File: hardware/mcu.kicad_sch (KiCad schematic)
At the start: 27 parts, among them J6 Debug, SW1 BOOT, SW2 RESET, U3 STM32F405RGTx, Y1 8MHz

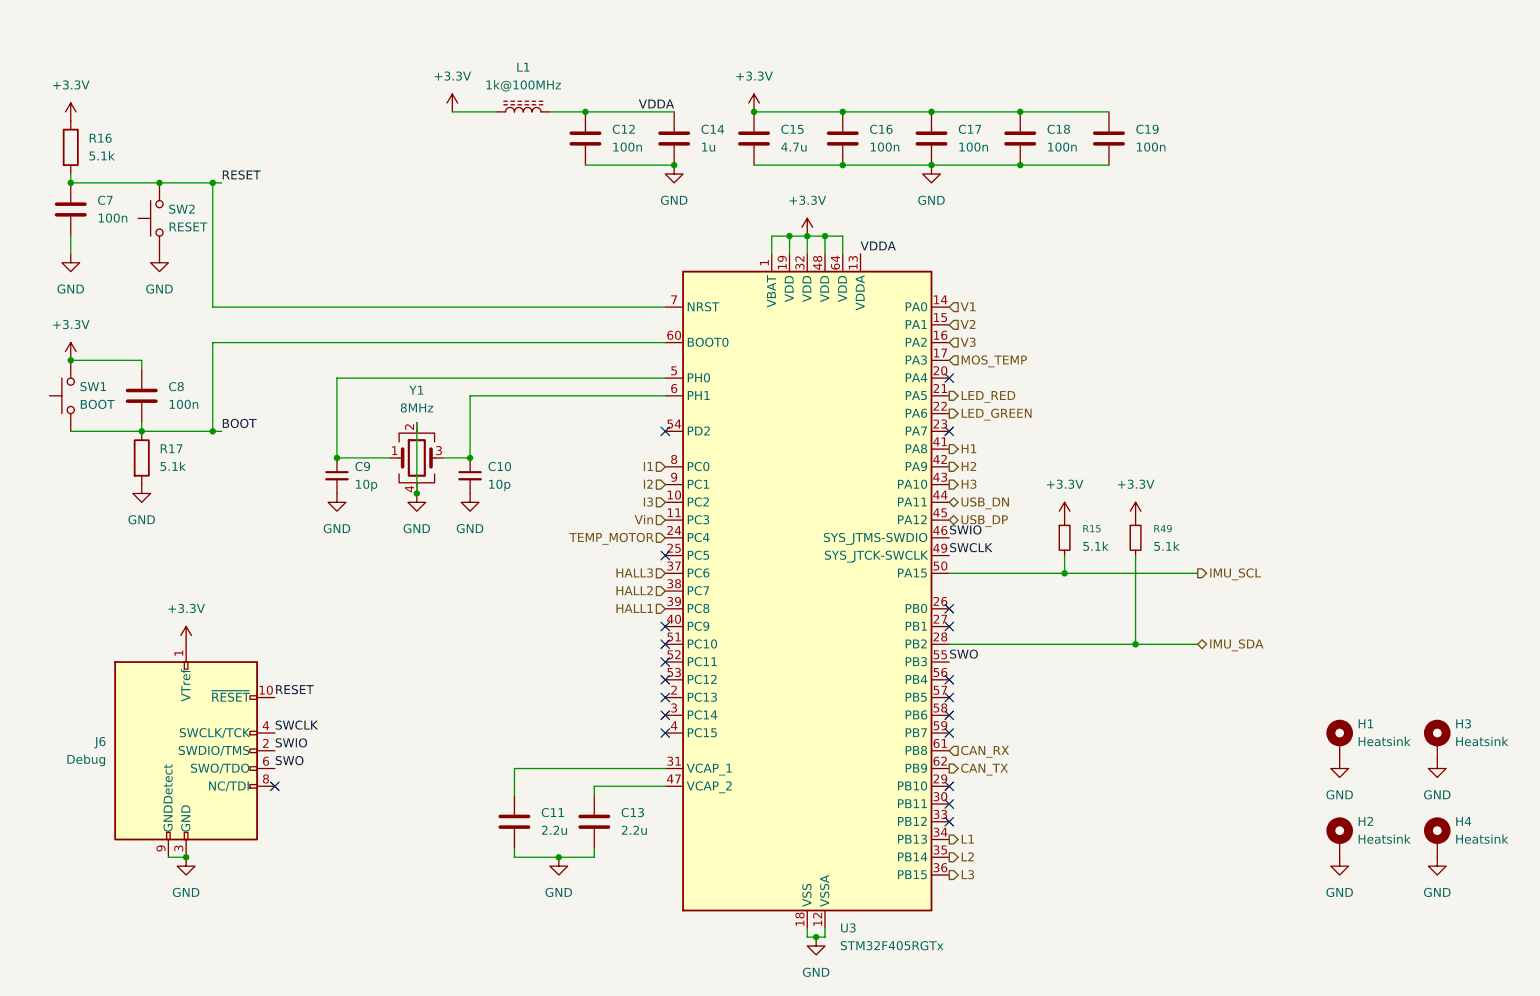
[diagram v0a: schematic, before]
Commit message: TVS and eletrolythic cap
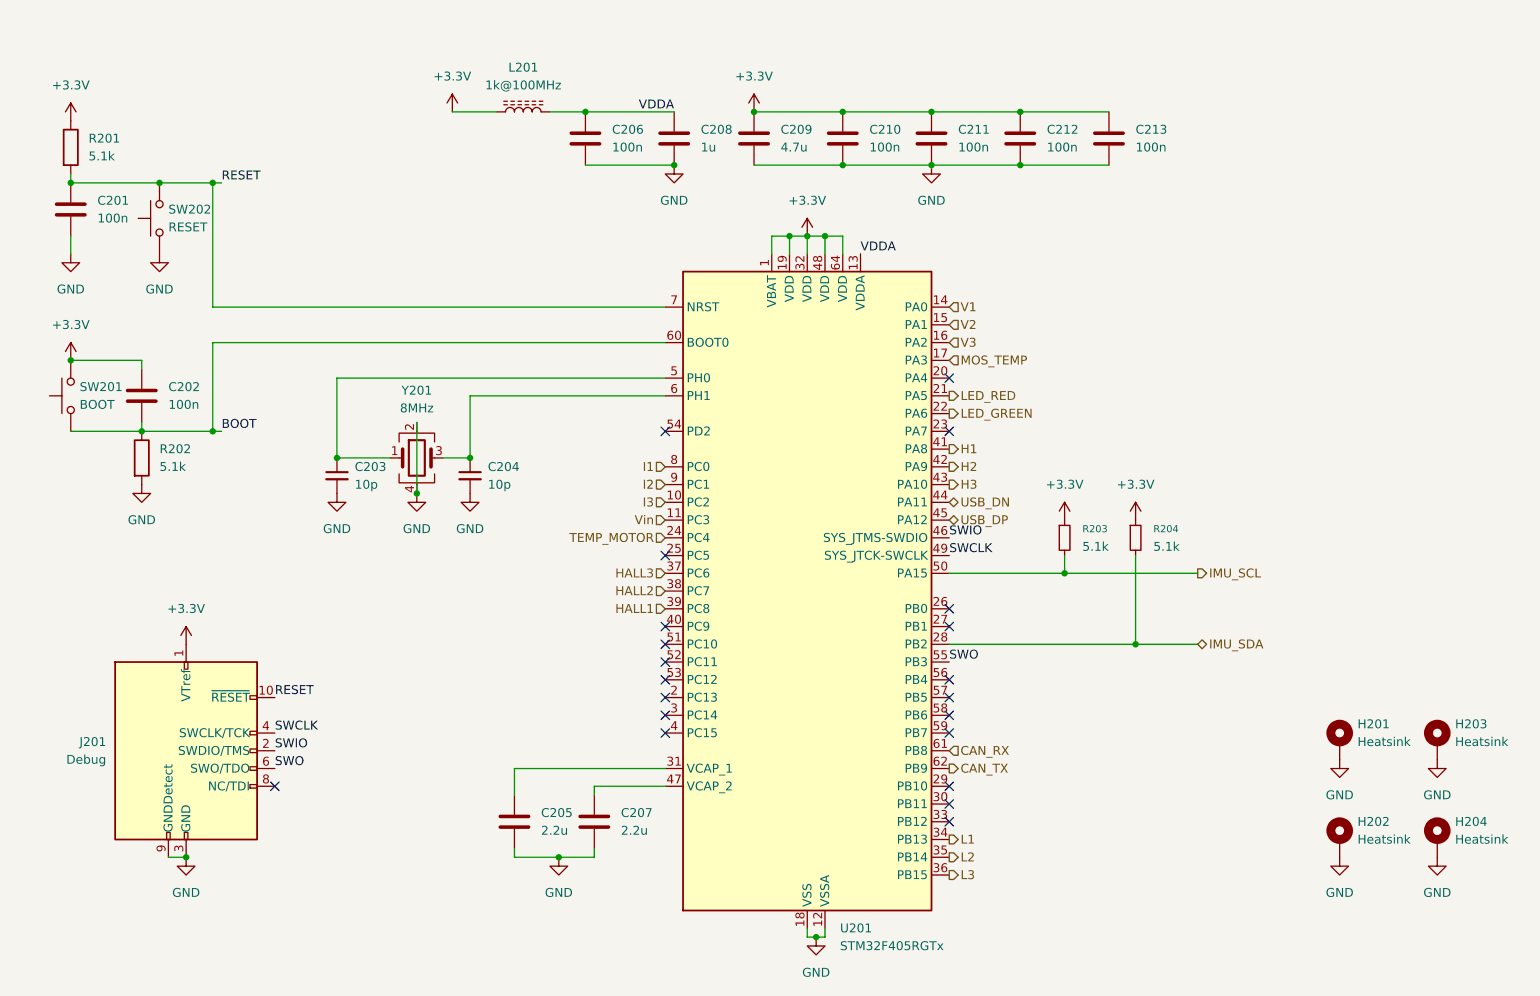
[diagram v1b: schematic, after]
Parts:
- renumbered C7 to C201, C8 to C202, C9 to C203, C10 to C204, C11 to C205, C12 to C206, C13 to C207, C14 to C208, C15 to C209, C16 to C210, C17 to C211, C18 to C212, C19 to C213, H1 to H201, H2 to H202, H3 to H203, H4 to H204, J6 to J201, L1 to L201, R16 to R201, R17 to R202, R15 to R203, R49 to R204, SW1 to SW201, SW2 to SW202, U3 to U201, Y1 to Y201

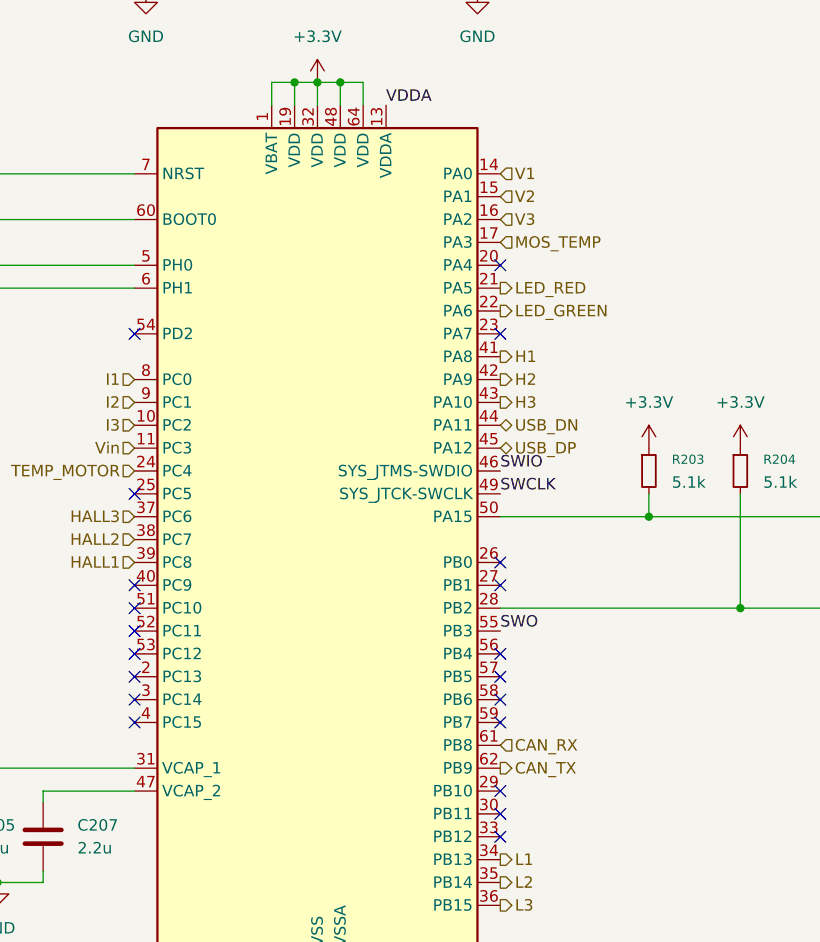
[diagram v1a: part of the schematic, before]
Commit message: Added external analog inputs
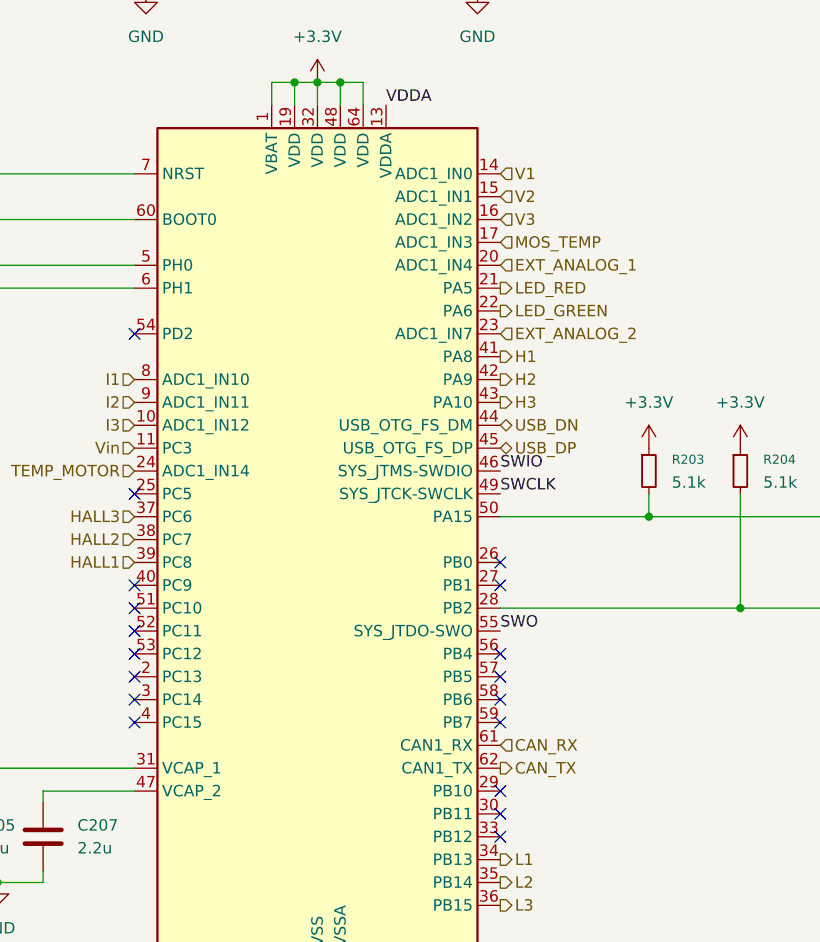
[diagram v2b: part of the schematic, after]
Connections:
- net EXT_ANALOG_1: now reaches U201.20 (PA4)
- net EXT_ANALOG_2: now reaches U201.23 (PA7)
- no-connect marks 21 -> 19
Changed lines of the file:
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@@
 	(title_block
 		(title "GreenMobi Drive")
-		(date "2025-07-02")
-		(rev "0.1")
+		(date "2025-09-09")
+		(rev "1.0")
 	)
 	(junction
@@
 	)
 	(no_connect
-		(at 187.96 72.39)
-	)
-	(no_connect
 		(at 187.96 107.95)
 	)
@@
 	)
 	(no_connect
-		(at 187.96 80.01)
-	)
-	(no_connect
 		(at 147.32 113.03)
 	)
@@
 		)
 	)
+	(hierarchical_label "EXT_ANALOG_2"
+		(shape input)
+		(at 187.96 80.01 0)
+		(effects
+			(font
+				(size 1.27 1.27)
+			)
+			(justify left)
+		)
+	)
 	(hierarchical_label "CAN_TX"
 		(shape output)
@@
 		)
 	)
+	(hierarchical_label "EXT_ANALOG_1"
+		(shape input)
+		(at 187.96 72.39 0)
+		(effects
+			(font
+				(size 1.27 1.27)
+			)
+			(justify left)
+		)
+	)
 	(hierarchical_label "I3"
 		(shape input)
@@
 		)
 		(pin "55"
+			(alternate "SYS_JTDO-SWO")
 		)
 		(pin "28"
 		)
 		(pin "62"
+			(alternate "CAN1_TX")
 		)
 		(pin "27"
@@
 		)
 		(pin "10"
+			(alternate "ADC1_IN12")
 		)
 		(pin "20"
+			(alternate "ADC1_IN4")
 		)
 		(pin "13"
 		)
 		(pin "61"
+			(alternate "CAN1_RX")
 		)
 		(pin "29"
 		)
 		(pin "16"
+			(alternate "ADC1_IN2")
 		)
 		(pin "45"
+			(alternate "USB_OTG_FS_DP")
 		)
 		(pin "53"
@@
 		)
 		(pin "17"
+			(alternate "ADC1_IN3")
 		)
 		(pin "3"
 		)
 		(pin "23"
+			(alternate "ADC1_IN7")
 		)
 		(pin "15"
+			(alternate "ADC1_IN1")
 		)
 		(pin "5"
@@
 		)
 		(pin "14"
+			(alternate "ADC1_IN0")
 		)
 		(pin "43"
@@
 		)
 		(pin "44"
+			(alternate "USB_OTG_FS_DM")
 		)
 		(pin "32"
@@
 		)
 		(pin "8"
+			(alternate "ADC1_IN10")
 		)
 		(pin "37"
 		)
 		(pin "9"
+			(alternate "ADC1_IN11")
 		)
 		(pin "4"
@@
 		)
 		(pin "24"
+			(alternate "ADC1_IN14")
 		)
 		(pin "52"

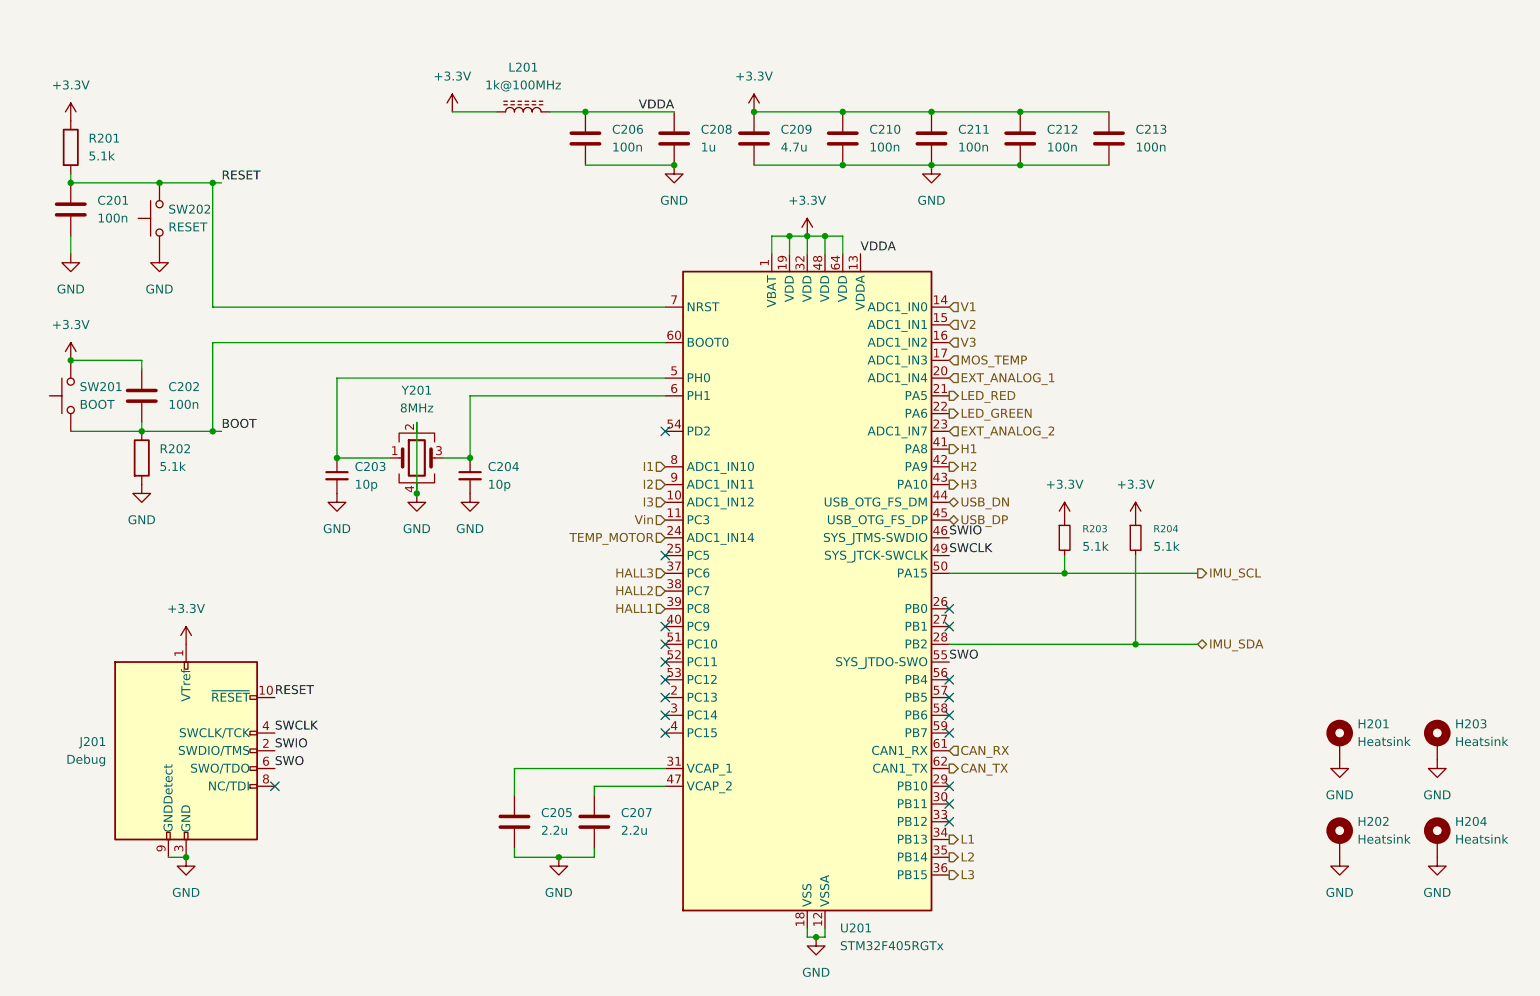
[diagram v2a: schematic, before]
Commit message: Removed buttons for boot and reset
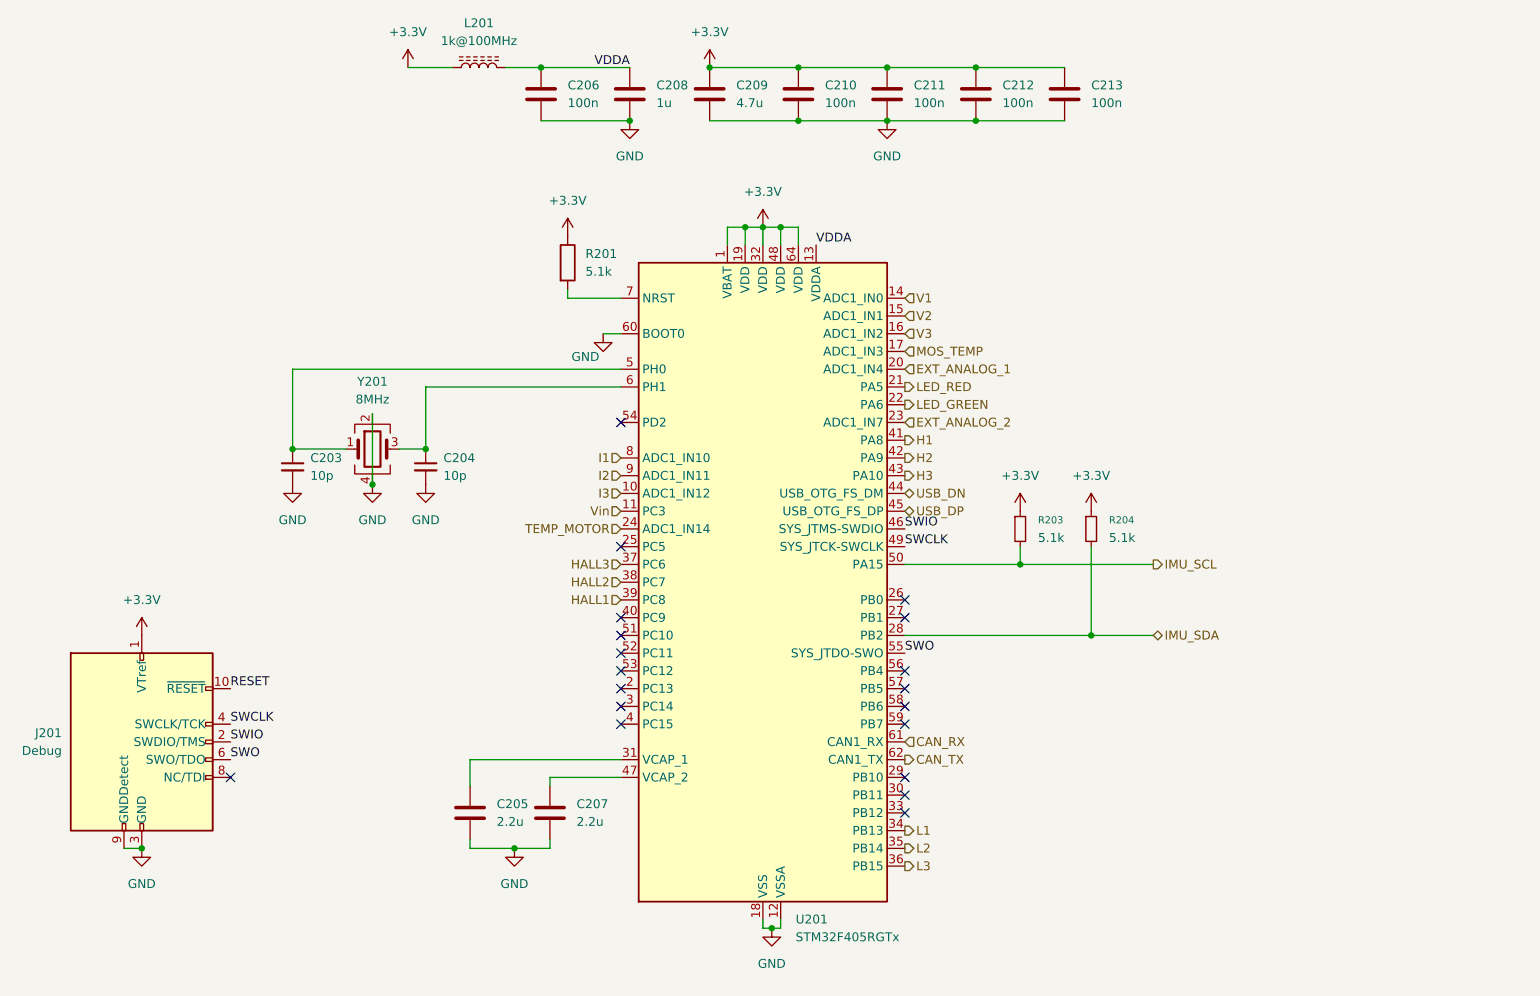
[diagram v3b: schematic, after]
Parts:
- removed C201, C202: 100n, Capacitor_SMD:C_0402_1005Metric, symbol Device:C
- removed H201, H202, H203, H204: Heatsink, MountingHole:MountingHole_3.2mm_M3_Pad, symbol Mechanical:MountingHole_Pad
- removed R202: 5.1k, Resistor_SMD:R_0402_1005Metric, symbol Device:R
- removed SW201: BOOT, Button_Switch_SMD:SW_Push_SPST_NO_Alps_SKRK, symbol Switch:SW_Push
- removed SW202: RESET, Button_Switch_SMD:SW_Push_SPST_NO_Alps_SKRK, symbol Switch:SW_Push
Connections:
- net BOOT is gone; now on net GND: U201.60 (BOOT0)
- net RESET: no longer R201.2, U201.7 (NRST)
- new net: R201.2, U201.7 (NRST)
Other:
- moved on the sheet: C203, C204, C205, C206, C207, C208, C209, C210, C211, C212, C213, J201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

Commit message: ERC exclusions
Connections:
- net RESET: now also R201.2, U201.7 (NRST)
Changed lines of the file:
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@@
+	)
+	(label "RESET"
+		(at 140.97 60.96 180)
+		(effects
+			(font
+				(size 1.27 1.27)
+			)
+			(justify right bottom)
+		)
 	)
 	(label "RESET"

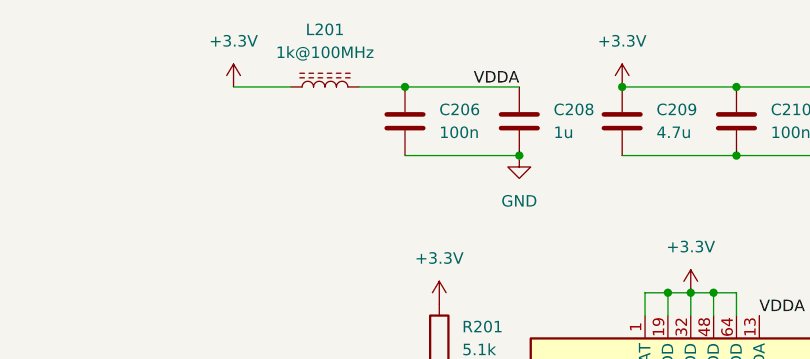
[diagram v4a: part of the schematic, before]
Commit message: Reduce board size
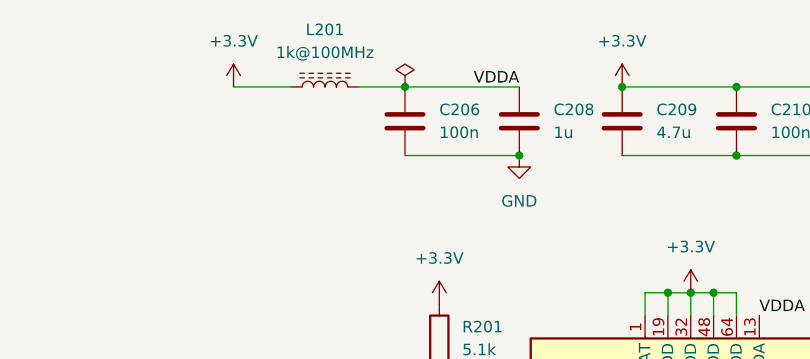
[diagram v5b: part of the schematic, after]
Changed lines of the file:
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@@
+	)
+	(symbol
+		(lib_id "power:PWR_FLAG")
+		(at 129.54 27.94 0)
+		(unit 1)
+		(exclude_from_sim no)
+		(in_bom yes)
+		(on_board yes)
+		(dnp no)
+		(fields_autoplaced yes)
+		(property "Reference" "#FLG0201"
+			(at 129.54 26.035 0)
+			(effects
+				(font
+					(size 1.27 1.27)
+				)
+				(hide yes)
+			)
+		)
+		(property "Value" "PWR_FLAG"
+			(at 129.54 22.86 0)
+			(effects
+				(font
+					(size 1.27 1.27)
+				)
+				(hide yes)
+			)
+		)
+		(property "Footprint" ""
+			(at 129.54 27.94 0)
+			(effects
+				(font
+					(size 1.27 1.27)
+				)
+				(hide yes)
+			)
+		)
+		(property "Datasheet" "~"
+			(at 129.54 27.94 0)
+			(effects
+				(font
+					(size 1.27 1.27)
+				)
+				(hide yes)
+			)
+		)
+		(property "Description" "Special symbol for telling ERC where power comes from"
+			(at 129.54 27.94 0)
+			(effects
+				(font
+					(size 1.27 1.27)
+				)
+				(hide yes)
+			)
+		)
+		(pin "1"
+		)
+		(instances
+			(project "greenmobi-drive"
+				(path "/a12b77e7-bd0f-4a70-9ba2-19a87ce48819/7c031b43-26d1-47e4-bdd2-d28a8add82c7"
+					(reference "#FLG0201")
+					(unit 1)
+				)
+			)
+		)
 	)
 	(symbol
